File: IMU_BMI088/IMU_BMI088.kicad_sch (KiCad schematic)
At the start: 3 parts, among them IC5 BMI088

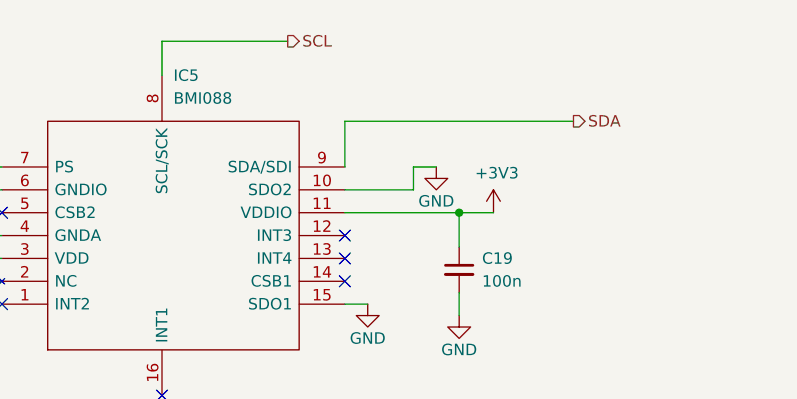
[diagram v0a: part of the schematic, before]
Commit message: Route sensors, IMU and radio board
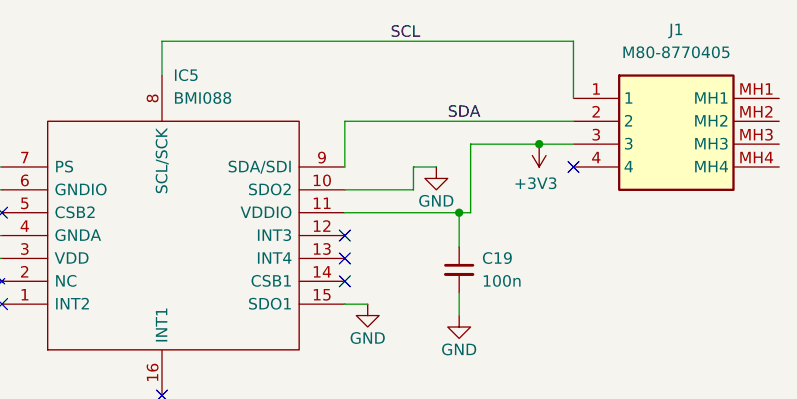
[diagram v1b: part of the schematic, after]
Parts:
- added J1: M80-8770405, M808770405, symbol M80-8770405:M80-8770405
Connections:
- net +3V3: now also J1.3
- net SCL: now also J1.1
- net SDA: now also J1.2
- no-connect marks 6 -> 7
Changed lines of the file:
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@@
   (junction (at 102.87 86.36) (diameter 0) (color 0 0 0 0)
   )
+  (junction (at 184.15 73.66) (diameter 0) (color 0 0 0 0)
+  )
+  (no_connect (at 187.96 76.2))
   (no_connect (at 162.56 86.36))
   (no_connect (at 124.46 81.28))
@@
     (stroke (width 0) (type default))
   )
+  (wire (pts (xy 176.53 73.66) (xy 176.53 81.28))
+    (stroke (width 0) (type default))
+  )
+  (wire (pts (xy 187.96 73.66) (xy 184.15 73.66))
+    (stroke (width 0) (type default))
+  )
   (wire (pts (xy 100.33 83.82) (xy 100.33 81.28))
     (stroke (width 0) (type default))
   )
+  (wire (pts (xy 187.96 62.23) (xy 187.96 68.58))
+    (stroke (width 0) (type default))
+  )
   (wire (pts (xy 170.18 76.2) (xy 172.72 76.2))
     (stroke (width 0) (type default))
@@
     (stroke (width 0) (type default))
   )
-  (wire (pts (xy 142.24 62.23) (xy 156.21 62.23))
+  (wire (pts (xy 142.24 62.23) (xy 187.96 62.23))
     (stroke (width 0) (type default))
   )
@@
     (stroke (width 0) (type default))
   )
-  (wire (pts (xy 175.26 81.28) (xy 179.07 81.28))
+  (wire (pts (xy 184.15 73.66) (xy 176.53 73.66))
+    (stroke (width 0) (type default))
+  )
+  (wire (pts (xy 175.26 81.28) (xy 176.53 81.28))
     (stroke (width 0) (type default))
   )
@@
     (stroke (width 0) (type default))
   )
-  (hierarchical_label "SCL" (shape output) (at 156.21 62.23 0) (fields_autoplaced)
-    (effects (font (size 1.27 1.27)) (justify left))
-  )
-  (hierarchical_label "SDA" (shape output) (at 187.96 71.12 0) (fields_autoplaced)
-    (effects (font (size 1.27 1.27)) (justify left))
+  (label "SDA" (at 173.99 71.12 0) (fields_autoplaced)
+    (effects (font (size 1.27 1.27)) (justify left bottom))
+  )
+  (label "SCL" (at 167.64 62.23 0) (fields_autoplaced)
+    (effects (font (size 1.27 1.27)) (justify left bottom))
   )
   (symbol (lib_id "power:GND") (at 172.72 76.2 0) (unit 1)
@@
     )
   )
-  (symbol (lib_id "power:+3V3") (at 179.07 81.28 0) (unit 1)
+  (symbol (lib_id "power:+3V3") (at 184.15 73.66 180) (unit 1)
     (in_bom yes) (on_board yes) (dnp no)
-    (property "Reference" "#PWR09" (at 179.07 85.09 0)
-      (effects (font (size 1.27 1.27)) hide)
-    )
-    (property "Value" "+3V3" (at 179.451 76.8858 0)
-      (effects (font (size 1.27 1.27)))
-    )
-    (property "Footprint" "" (at 179.07 81.28 0)
-      (effects (font (size 1.27 1.27)) hide)
-    )
-    (property "Datasheet" "" (at 179.07 81.28 0)
+    (property "Reference" "#PWR09" (at 184.15 69.85 0)
+      (effects (font (size 1.27 1.27)) hide)
+    )
+    (property "Value" "+3V3" (at 183.769 78.0542 0)
+      (effects (font (size 1.27 1.27)))
+    )
+    (property "Footprint" "" (at 184.15 73.66 0)
+      (effects (font (size 1.27 1.27)) hide)
+    )
+    (property "Datasheet" "" (at 184.15 73.66 0)
       (effects (font (size 1.27 1.27)) hide)
     )
@@
         )
       )
+    )
+  )
+  (symbol (lib_id "M80-8770405:M80-8770405") (at 187.96 68.58 0) (unit 1)
+    (in_bom yes) (on_board yes) (dnp no) (fields_autoplaced)
+    (property "Reference" "J1" (at 199.39 60.96 0)
+      (effects (font (size 1.27 1.27)))
+    )
+    (property "Value" "M80-8770405" (at 199.39 63.5 0)
+      (effects (font (size 1.27 1.27)))
+    )
+    (property "Footprint" "M808770405" (at 207.01 163.5 0)
+      (effects (font (size 1.27 1.27)) (justify left top) hide)
+    )
+    (property "Datasheet" "https://cdn.harwin.com/pdfs/M80-877.pdf" (at 207.01 263.5 0)
+      (effects (font (size 1.27 1.27)) (justify left top) hide)
+    )
+    (property "Height" "5.56" (at 207.01 463.5 0)
+      (effects (font (size 1.27 1.27)) (justify left top) hide)
+    )
+    (property "Manufacturer_Name" "Harwin" (at 207.01 563.5 0)
+      (effects (font (size 1.27 1.27)) (justify left top) hide)
+    )
+    (property "Manufacturer_Part_Number" "M80-8770405" (at 207.01 663.5 0)
+      (effects (font (size 1.27 1.27)) (justify left top) hide)
+    )
+    (property "Mouser Part Number" "855-M80-8770405" (at 207.01 763.5 0)
+      (effects (font (size 1.27 1.27)) (justify left top) hide)
+    )
+    (property "Mouser Price/Stock" "https://www.mouser.co.uk/ProductDetail/Harwin/M80-8770405?qs=3tymCvhQ29ZPq83M%252Bf8kIA%3D%3D" (at 207.01 863.5 0)
+      (effects (font (size 1.27 1.27)) (justify left top) hide)
+    )
+    (property "Arrow Part Number" "" (at 207.01 963.5 0)
+      (effects (font (size 1.27 1.27)) (justify left top) hide)
+    )
+    (property "Arrow Price/Stock" "" (at 207.01 1063.5 0)
+      (effects (font (size 1.27 1.27)) (justify left top) hide)
+    )
+    (pin "1")
+    (pin "2")
+    (pin "3")
+    (pin "4")
+    (pin "MH1")
+    (pin "MH2")
+    (pin "MH3")
+    (pin "MH4")
+    (instances
+      (project "IMU_BMI088"
+        (path "/6dc614db-ec47-403a-a60b-436d28a59059"
+          (reference "J1") (unit 1)
+        )
+      )

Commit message: Done with most of the boards
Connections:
- net GND: now also J1.4
- no-connect marks 7 -> 10
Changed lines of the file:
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@@
   (junction (at 184.15 73.66) (diameter 0) (color 0 0 0 0)
   )
-  (no_connect (at 187.96 76.2))
   (no_connect (at 162.56 86.36))
   (no_connect (at 124.46 81.28))
   (no_connect (at 142.24 101.6))
   (no_connect (at 162.56 88.9))
+  (no_connect (at 210.82 76.2))
   (no_connect (at 162.56 83.82))
+  (no_connect (at 210.82 73.66))
+  (no_connect (at 210.82 71.12))
   (no_connect (at 124.46 91.44))
+  (no_connect (at 210.82 68.58))
+  (wire (pts (xy 187.96 76.2) (xy 187.96 81.28))
+    (stroke (width 0) (type default))
+  )
   (wire (pts (xy 87.63 76.2) (xy 124.46 76.2))
     (stroke (width 0) (type default))
@@
         )
       )
+    )
+  )
+  (symbol (lib_id "power:GND") (at 187.96 81.28 0) (unit 1)
+    (in_bom yes) (on_board yes) (dnp no)
+    (property "Reference" "#PWR03" (at 187.96 87.63 0)
+      (effects (font (size 1.27 1.27)) hide)
+    )
+    (property "Value" "GND" (at 187.96 85.09 0)
+      (effects (font (size 1.27 1.27)))
+    )
+    (property "Footprint" "" (at 187.96 81.28 0)
+      (effects (font (size 1.27 1.27)) hide)
+    )
+    (property "Datasheet" "" (at 187.96 81.28 0)
+      (effects (font (size 1.27 1.27)) hide)
+    )
+    (pin "1")
+    (instances
+      (project "Flight_Computer_V2"
+        (path "/39d7ebb3-b69d-4ae9-8f55-c9acfe77d345/4a05f57f-ad7d-4317-b08f-5601038a99f3"
+          (reference "#PWR03") (unit 1)
+        )
+        (path "/39d7ebb3-b69d-4ae9-8f55-c9acfe77d345/d063216e-e605-415c-b172-b63dbdfef200"
+          (reference "#PWR050") (unit 1)
+        )
+      )
+      (project "STM32F405RGT6"
+        (path "/6135eb53-87c0-4516-a6dc-aa2a3e58fdeb"
+          (reference "#PWR03") (unit 1)
+        )
+      )
+      (project "IMU_BMI088"
+        (path "/6dc614db-ec47-403a-a60b-436d28a59059"
+          (reference "#PWR011") (unit 1)
+        )
+      )
+      (project "avionics_flight_computer"
+        (path "/b1d299c5-d712-4abd-abfc-85bf9dc0241e/1d0982b1-a7f8-42e4-83d7-31334d6351d0"
+          (reference "#PWR03") (unit 1)
+        )
+      )

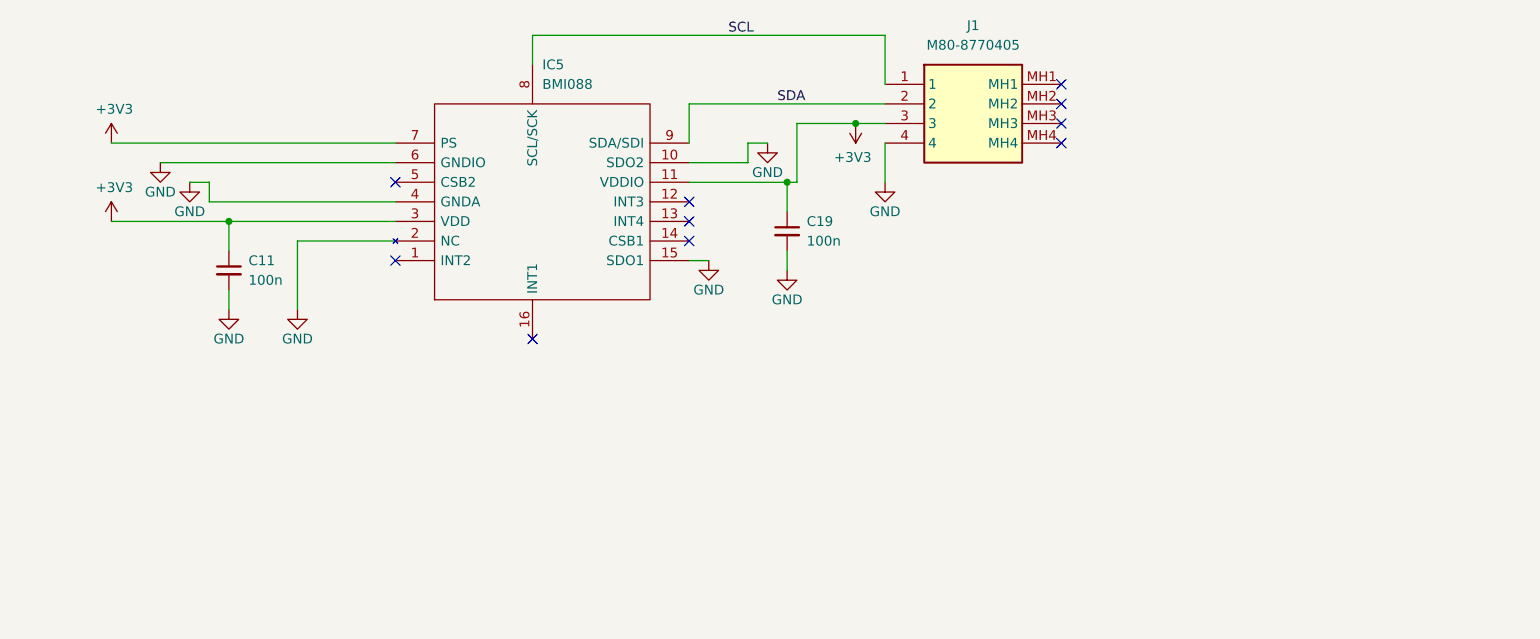
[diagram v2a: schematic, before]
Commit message: Fixed Accel, Barometer, FRAM, Inertia unit, and Magnetometer
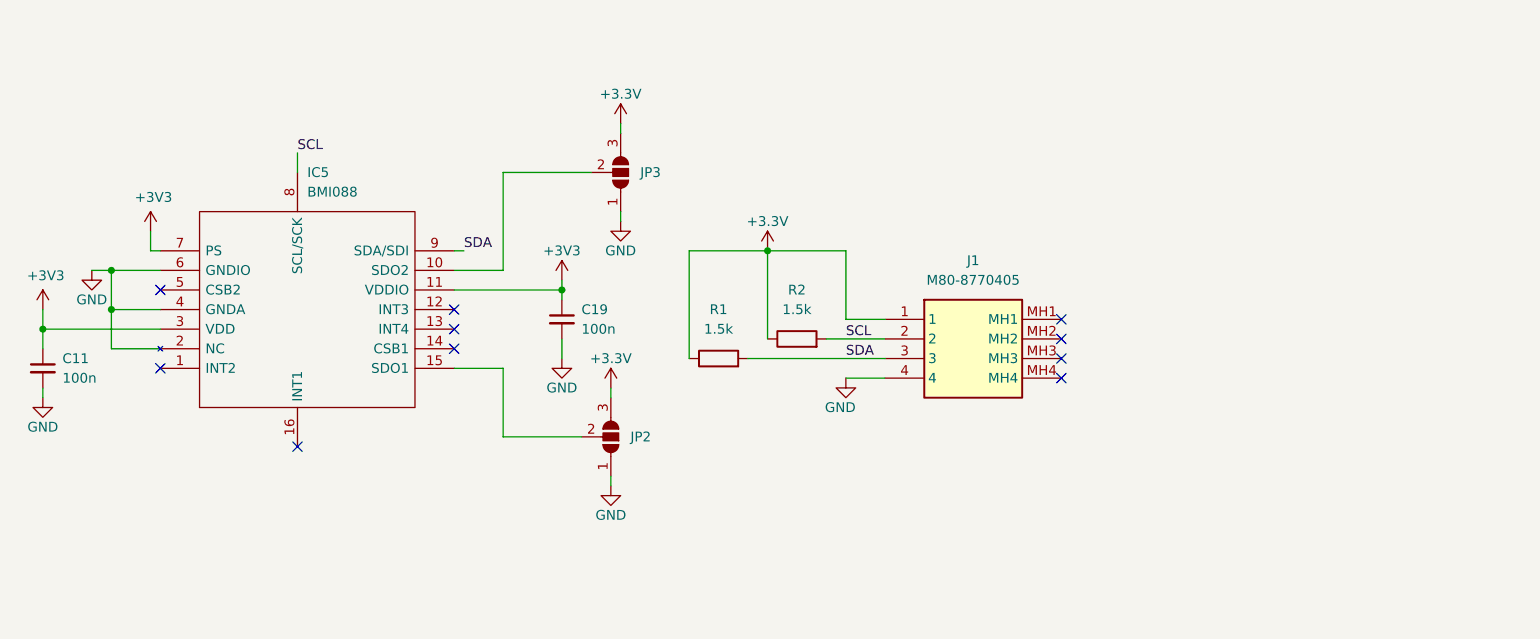
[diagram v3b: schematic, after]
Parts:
- added JP2, JP3: SolderJumper_3_Open, Jumper:SolderJumper-3_P1.3mm_Open_RoundedPad1.0x1.5mm_NumberLabels, symbol Jumper:SolderJumper_3_Open
- added R1, R2: 1.5k, Resistor_SMD:R_0201_0603Metric_Pad0.64x0.40mm_HandSolder, symbol Device:R
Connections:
- net +3V3: no longer J1.3
- net GND: now also JP2.1 (A), JP3.1 (A); no longer IC5.10 (SDO2), IC5.15 (SDO1)
- net SCL: now also J1.2, R2.2; no longer J1.1
- net SDA: now also J1.3, R1.2; no longer J1.2
- new net: IC5.15 (SDO1), JP2.2 (C)
- new net: IC5.10 (SDO2), JP3.2 (C)
- new net +3.3V: J1.1, JP2.3 (B), JP3.3 (B), R1.1, R2.1
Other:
- company: (none) -> USST Avionics
- title: (none) -> Inertial Unit BMI088
- moved on the sheet: C11, C19, IC5

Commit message: LC24 PCBs
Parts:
- removed J1: M80-8770405, M808770405, symbol M80-8770405:M80-8770405
- added H1, H2, H3, H4: MountingHole_Pad, Mounting_Wuerth:Mounting_Wuerth_WA-SMSI-M1.6_H1mm_9774010633, symbol Mechanical:MountingHole_Pad
- added J1: M80-8770422, Harwin-M80-8770422:CONN_M80-87704_HRW, symbol Harwin-M80-8770422:M80-8770422
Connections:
- net +3V3 is gone; now on net +3.3V: C11.1, C19.1, IC5.11 (VDDIO), IC5.3 (VDD), IC5.7 (PS)
- net +3.3V: now also J1.1
- net GND: now also H1.1, H2.1, H3.1, H4.1, J1.4
- net SCL: now also J1.2
- net SDA: now also J1.3
- no-connect marks 10 -> 6
